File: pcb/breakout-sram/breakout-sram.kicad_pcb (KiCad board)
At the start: 4 copper layers, 62 x 62 mm, 7 parts, among them J1 FX18-120P-0.8SV20, J2 FX18-120S-0.8SV20, U1 IS61WV102416DBLL-10TLI

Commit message: [pcb][pmod] remove stale ref from pcb
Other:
- board text added: "https://github.com/pbozeman/vanilla-ice40"
- board text added: "https://pbozeman.dev"
- board text removed: "git@github.com:pbozeman/vanilla-ice40.git"
- board text removed: "www.pbozeman.dev"
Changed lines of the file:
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@@
 			)
 		)
+		(property "LCSC Part #" "C3650293"
+			(at 0 0 -90)
+			(unlocked yes)
+			(layer "F.Fab")
+			(hide yes)
+			(effects
+				(font
+					(size 1 1)
+					(thickness 0.15)
+				)
+			)
+		)
 		(property ki_fp_filters "CONN_120P-0.8SV20")
 		(sheetname "Root")
@@
 			)
 		)
+		(property "LCSC Part #" "C598059"
+			(at 0 0 -90)
+			(unlocked yes)
+			(layer "F.Fab")
+			(hide yes)
+			(effects
+				(font
+					(size 1 1)
+					(thickness 0.15)
+				)
+			)
+		)
 		(property ki_fp_filters "CONN_120S-0.8SV20")
 		(sheetname "Root")
@@
 			)
 		)
-		(property "Footprint" "IS61WV102416DBLLIS61WV102416DBLL:IS61WV102416DBLL-10TLI_ISI"
+		(property "Footprint" "IS61WV102416DBLL-10TLI_ISI"
 			(at 0 0 0)
 			(unlocked yes)
@@
 		(fp_text user "*"
 			(at -8.9154 -6.0198 0)
-			(unlocked yes)
 			(layer "F.Fab")
 			(effects
@@
 			)
 		)
-		(fp_text user "*"
-			(at -8.9154 -6.0198 0)
+		(fp_text user "${REFERENCE}"
+			(at 0 0 0)
+			(unlocked yes)
 			(layer "F.Fab")
 			(effects
@@
 			)
 		)
-		(fp_text user "${REFERENCE}"
-			(at 0 0 0)
+		(fp_text user "*"
+			(at -8.9154 -6.0198 0)
 			(unlocked yes)
 			(layer "F.Fab")
@@
 		(layer "Edge.Cuts")
 	)
-	(gr_text "www.pbozeman.dev"
-		(at 101.573965 100 -0)
+	(gr_text "https://pbozeman.dev"
+		(at 101.573965 100 0)
 		(layer "B.SilkS")
 		(effects
@@
 		)
 	)
-	(gr_text "git@github.com:pbozeman/vanilla-ice40.git"
+	(gr_text "https://github.com/pbozeman/vanilla-ice40"
 		(at 101.573965 101.1 0)
 		(layer "B.SilkS")

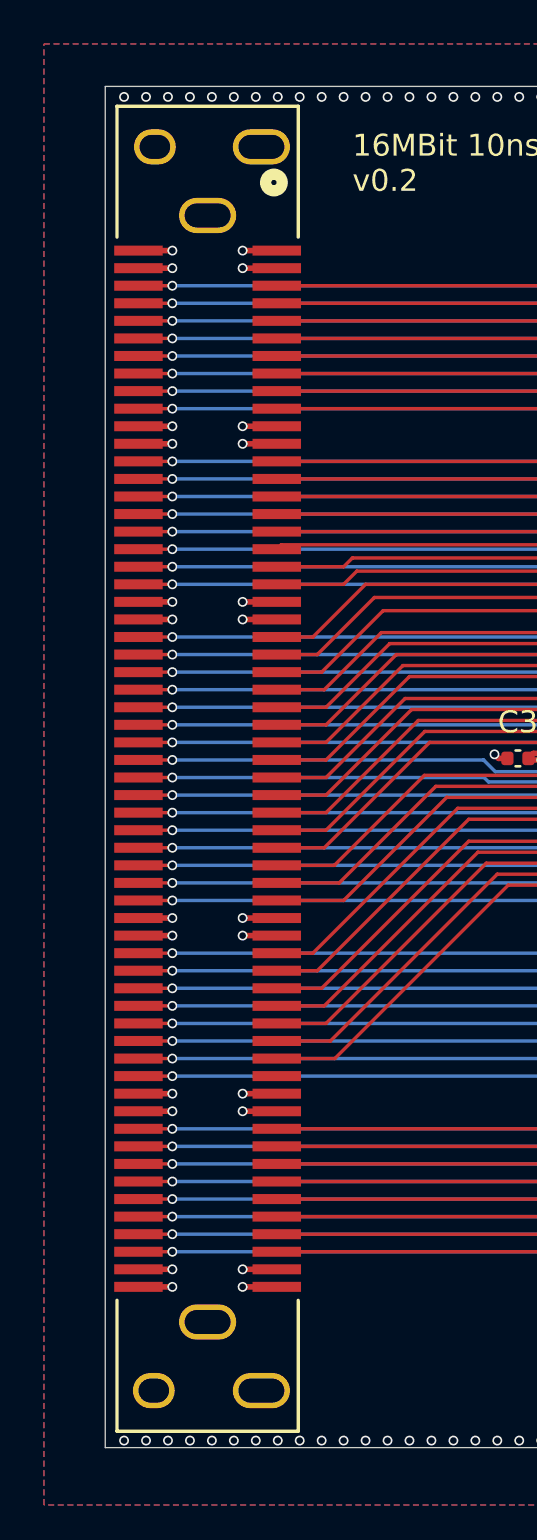
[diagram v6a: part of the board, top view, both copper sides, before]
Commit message: [pcb] add FX18-120P footprint and update pcbs
and a few adc fixes, including a key resistor fix
(the op amp for Y had a copy paste error from X
on the positive Rg)
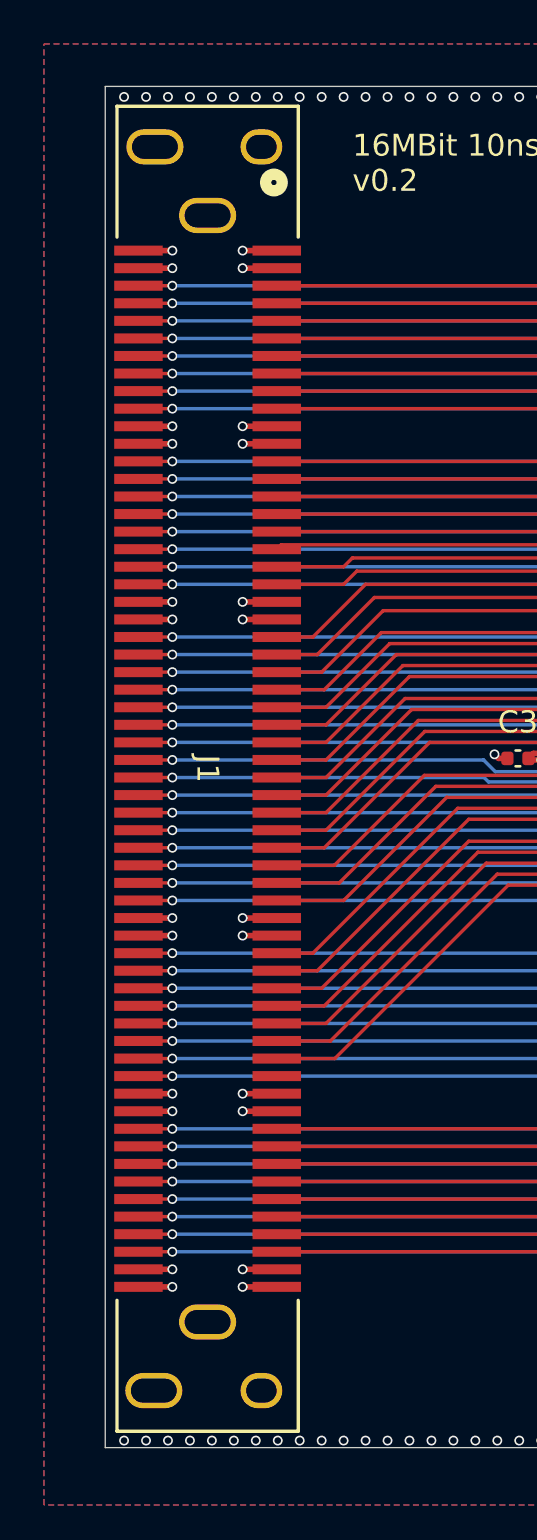
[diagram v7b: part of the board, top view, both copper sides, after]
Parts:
- J1: footprint custom:CUSTOM_FX_120S-0.8SH20 -> custom:CUSTOM_FX_120P-0.8SH20
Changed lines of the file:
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@@
 		)
 	)
-	(footprint "custom:CUSTOM_FX_120S-0.8SH20"
+	(footprint "custom:CUSTOM_FX_120P-0.8SH20"
 		(layer "F.Cu")
 		(at 55.805 72.599999 -90)
 		(tags "FX18-120S-0.8SV20 ")
 		(property "Reference" "J1"
-			(at -27.57 -6.489999 0)
+			(at 0 0 -90)
 			(unlocked yes)
 			(layer "F.SilkS")
-			(hide yes)
 			(effects
 				(font
@@
 			)
 		)
-		(property "Footprint" "custom:CUSTOM_FX_120S-0.8SH20"
+		(property "Footprint" "custom:CUSTOM_FX_120P-0.8SH20"
 			(at 0 0 -90)
 			(unlocked yes)
@@
 		)
 		(pad "121" thru_hole oval
-			(at -28.325 2.4)
+			(at -28.325 -2.45)
 			(size 1.908 1.608)
 			(drill oval 1.4 1.1)
@@
 		)
 		(pad "122" thru_hole oval
-			(at -28.325 -2.45)
+			(at -28.325 2.4)
 			(size 2.608001 1.608)
 			(drill oval 2.1 1.1)
@@
 		)
 		(pad "125" thru_hole oval
-			(at 28.325 2.45)
+			(at 28.325 -2.45)
 			(size 1.908 1.608)
 			(drill oval 1.4 1.1)
@@
 		)
 		(pad "126" thru_hole oval
-			(at 28.325 -2.45)
+			(at 28.325 2.45)
 			(size 2.608001 1.608)
 			(drill oval 2.1 1.1)
@@
 			)
 		)
-		(fp_text user "*"
-			(at -8.9154 -6.0198 0)
+		(fp_text user "${REFERENCE}"
+			(at 0 0 0)
+			(unlocked yes)
 			(layer "F.Fab")
 			(effects
@@
 			)
 		)
-		(fp_text user "${REFERENCE}"
-			(at 0 0 0)
-			(unlocked yes)
+		(fp_text user "*"
+			(at -8.9154 -6.0198 0)
 			(layer "F.Fab")
 			(effects

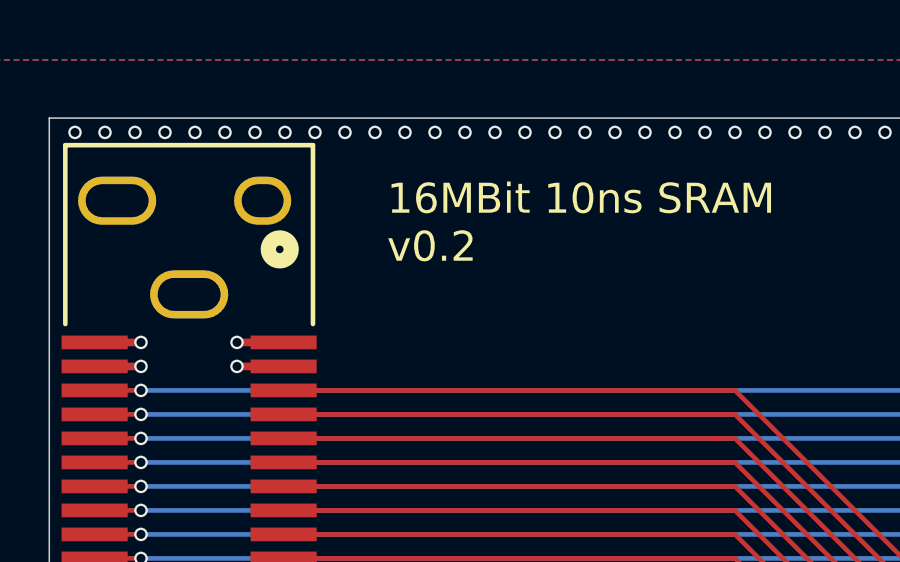
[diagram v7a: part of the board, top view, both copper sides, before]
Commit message: [pcb][sram] bump silkscreen version for updated footprint
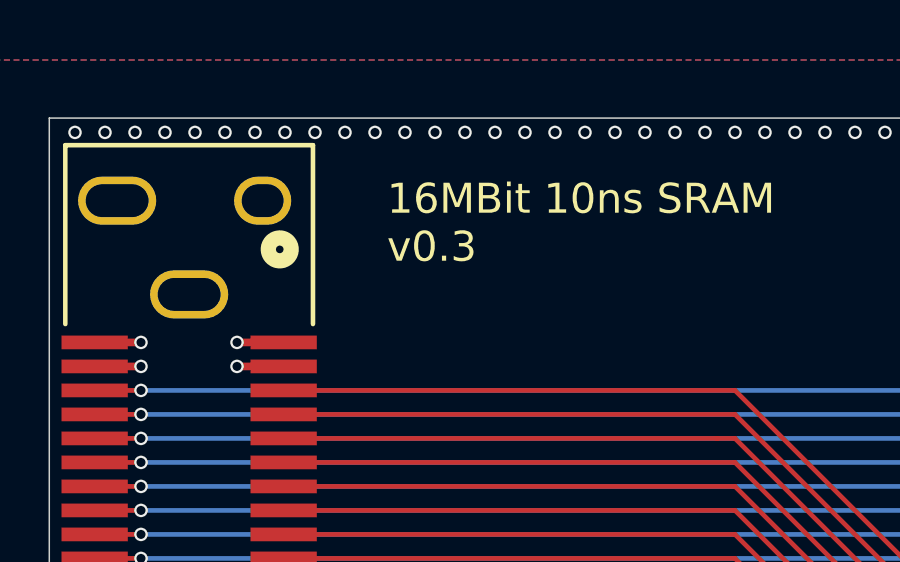
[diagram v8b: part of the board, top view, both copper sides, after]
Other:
- board text added: "v0.3"
- board text removed: "v0.2"
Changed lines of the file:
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@@
 		)
 	)
-	(gr_text "v0.2"
+	(gr_text "v0.3"
 		(at 62.4 46.4 0)
 		(layer "F.SilkS")
